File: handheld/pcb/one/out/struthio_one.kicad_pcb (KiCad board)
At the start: 2 copper layers, 68.2 x 105.5 mm, 12 parts, among them J1 Header_2x16_Waveshare, J2 S2B-PH-K-S, Q1 AO3401A, Q2 AO3400A, SW1 TS-1187A-B-A-B, SW2 TS-1187A-B-A-B, SW3 TS-1187A-B-A-B, SW4 TS-1187A-B-A-B, SW5 SS-12D06-G030

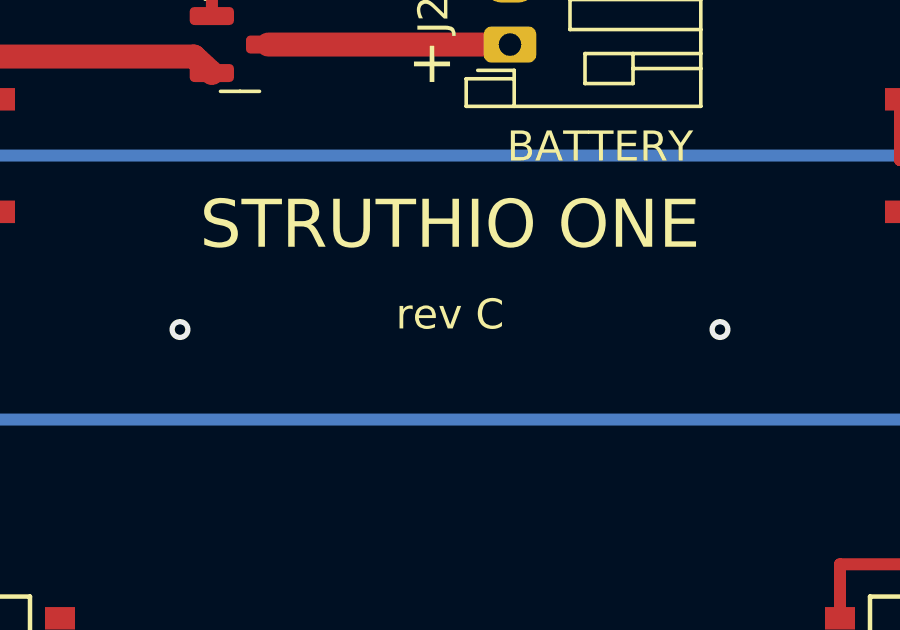
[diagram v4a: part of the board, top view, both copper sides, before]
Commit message: ONE SLIM rev S2 hardware (foolproof) and ONE board rev D
SLIM case: no slide switch; a printed plunger in the left wall presses the Waveshare's
PWR key; one screw size (5 x M2 x 6 countersunk); surface-mount battery socket (no
leads to trim); lead clips; pins stand 3.6 mm out so either socket height works
(3.6 / 2.5 mm into J8), no spacer, no measuring; keyed pin jig (fence + two pegs a
turned-over board cannot sit on) with an 11 mm axle gauge; panel jig. 61 checks pass.
SLIM board rev S2: SW1-4, J2 (C295747), Q1 only, all surface-mount; pin 9 open.
ONE board rev D: header pin 9 tied to GND (the firmware's model strap).
Both boards: DRC no errors, no unconnected pads.

Co-Authored-By: Claude Opus 5.5 <noreply@anthropic.com>
Claude-Session: https://claude.ai/code/session_01BN2x2AjDXTm5ZbuwkUnxX5
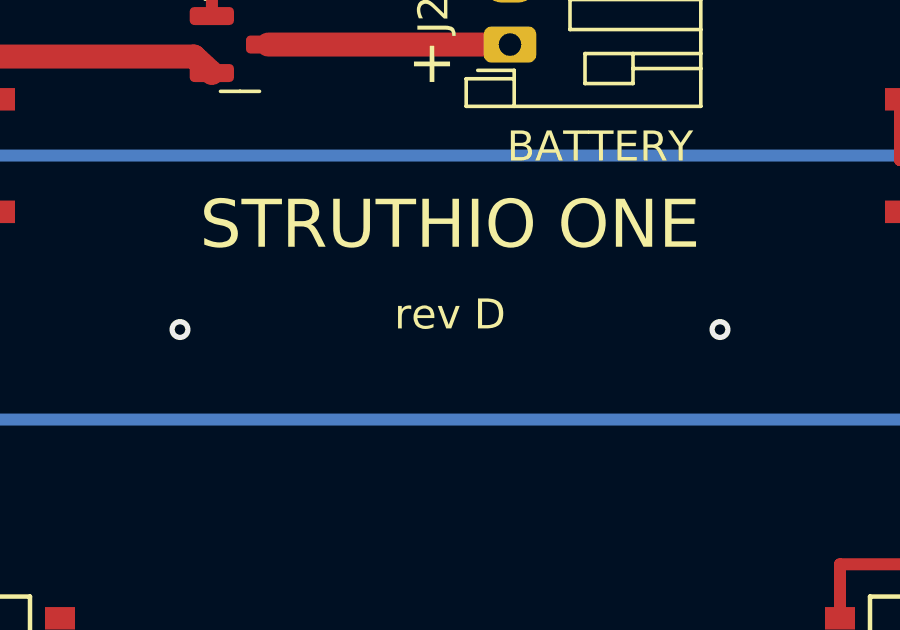
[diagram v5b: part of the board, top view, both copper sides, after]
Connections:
- J1 pad 9: (no net) -> GND
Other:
- board text added: "rev D"
- board text removed: "rev C"
